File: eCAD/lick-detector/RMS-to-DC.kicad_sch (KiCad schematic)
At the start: 23 parts, among them J4 J_PinHeader_01x02_2.54_V, J5 J_PinHeader_01x02_2.54_V, J6 J_PinHeader_01x02_2.54_V, U4 OPA2365, U5 OPA2365

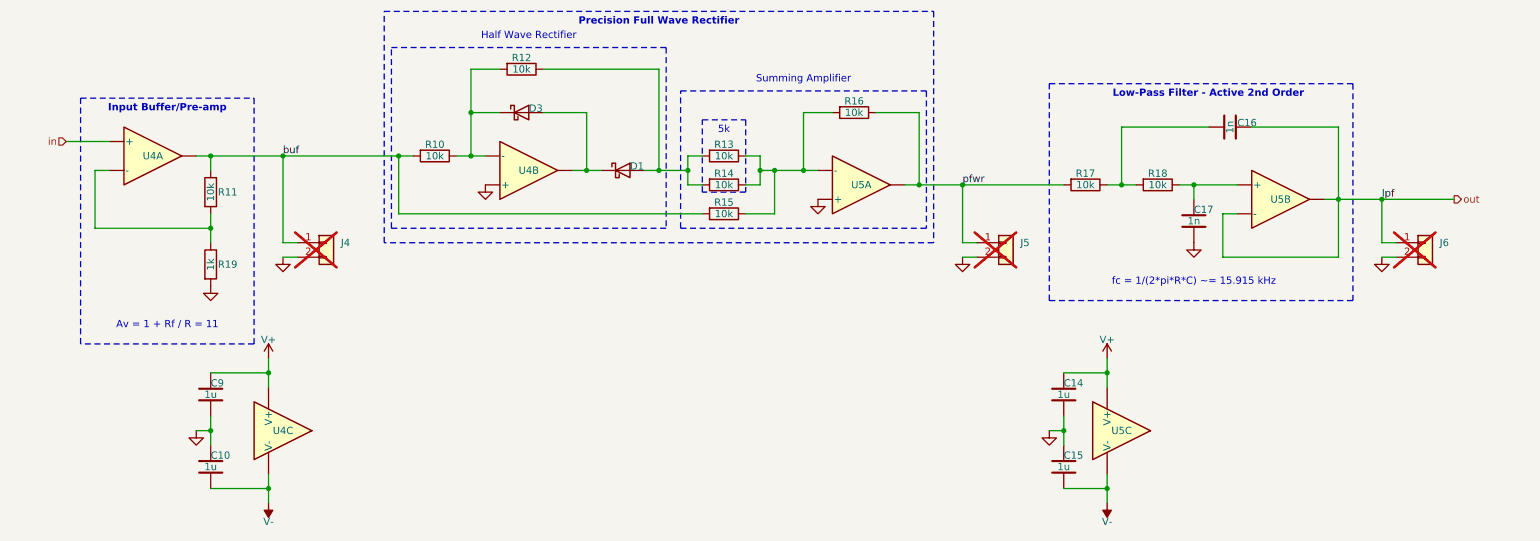
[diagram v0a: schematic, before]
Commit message: Number of upgrades complete: - Lower amplitude sine wave generator - Improved debug connector layout - Brightness of LED decreased - README updated with guide and areas for documentation - .gitignore added to ignore backup files and temporary files
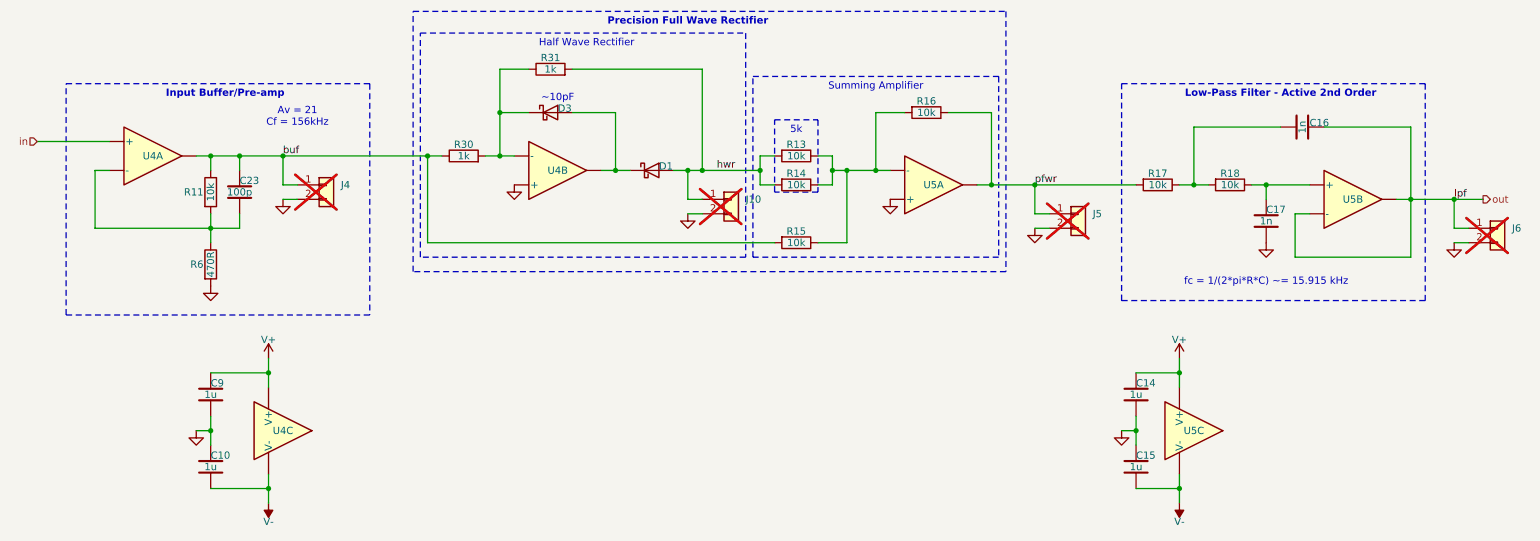
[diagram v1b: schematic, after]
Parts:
- removed R10, R12: 10k, !fablabs-kicad-library:R_0603_1608M, symbol !fablabs-kicad-library:R_0603_10k
- removed R19: 1k, !fablabs-kicad-library:R_0603_1608M, symbol !fablabs-kicad-library:R_0603_1k
- added C23: 100p, !fablabs-kicad-library:C_0603_1608M, symbol !fablabs-kicad-library:C_0603_100p_50V_C0G
- added J10: J_PinHeader_01x02_2.54_V, !fablabs-kicad-library:J_PinHeader_01x02_2.54_V, symbol !fablabs-kicad-library:J_PinHeader_01x02_2.54_V
- added R30, R31: 1k, !fablabs-kicad-library:R_0603_1608M, symbol !fablabs-kicad-library:R_0603_1k
- added R6: 470R, !fablabs-kicad-library:R_0603_1608M, symbol !fablabs-kicad-library:R_0603_470R
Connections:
- net GND: now also J10.2 (Pin_2), R6.1
- net buf: now also C23.2, R30.2
- net at R11.1, U4.2 (-): now also C23.1, R6.2
- net at D3.1 (K), U4.6 (-): now also R30.1, R31.2
- net hwr: now reaches D1.2 (A), R13.1, R14.1
- net hwr: now also J10.1 (Pin_1), R31.1
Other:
- note added: "Av = 21 Cf = 156kHz"
- note added: "~10pF"
- note removed: "Av = 1 + Rf / R = 11"
- moved on the sheet: C14, C15, C16, C17, D1, D3, J4, J5, J6, R13, R14, R15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
